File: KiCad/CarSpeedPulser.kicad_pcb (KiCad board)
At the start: 2 copper layers, 48 x 48 mm, 24 parts, among them P1 CONN_01X03, P2 CONN_01X05, Q1 RUE002N02, SW1 RESET, SW2 UP, SW3 DOWN, U1 LPC810, U2 AQM0802A-RN-GBW, U3 NJU7223DL1-33, U4 BD45231G

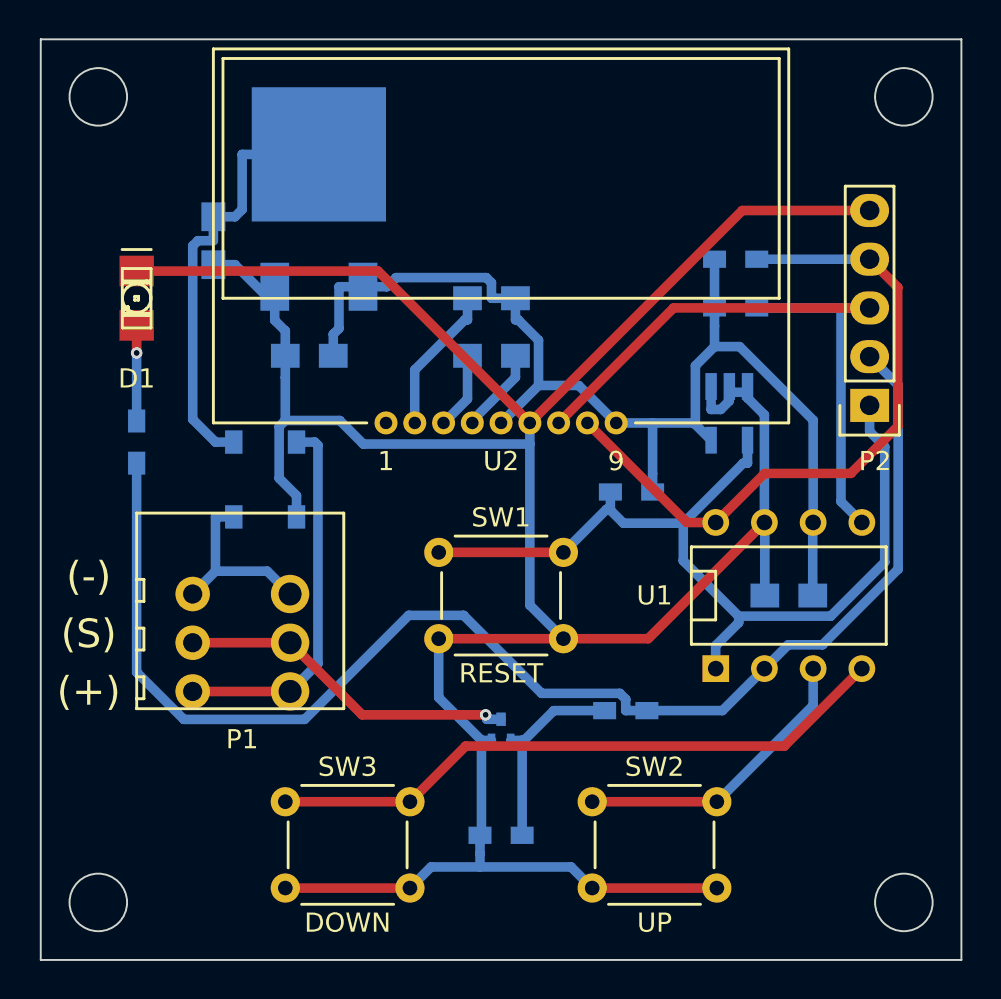
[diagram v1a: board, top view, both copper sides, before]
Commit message: Replaced 3.3V regulator
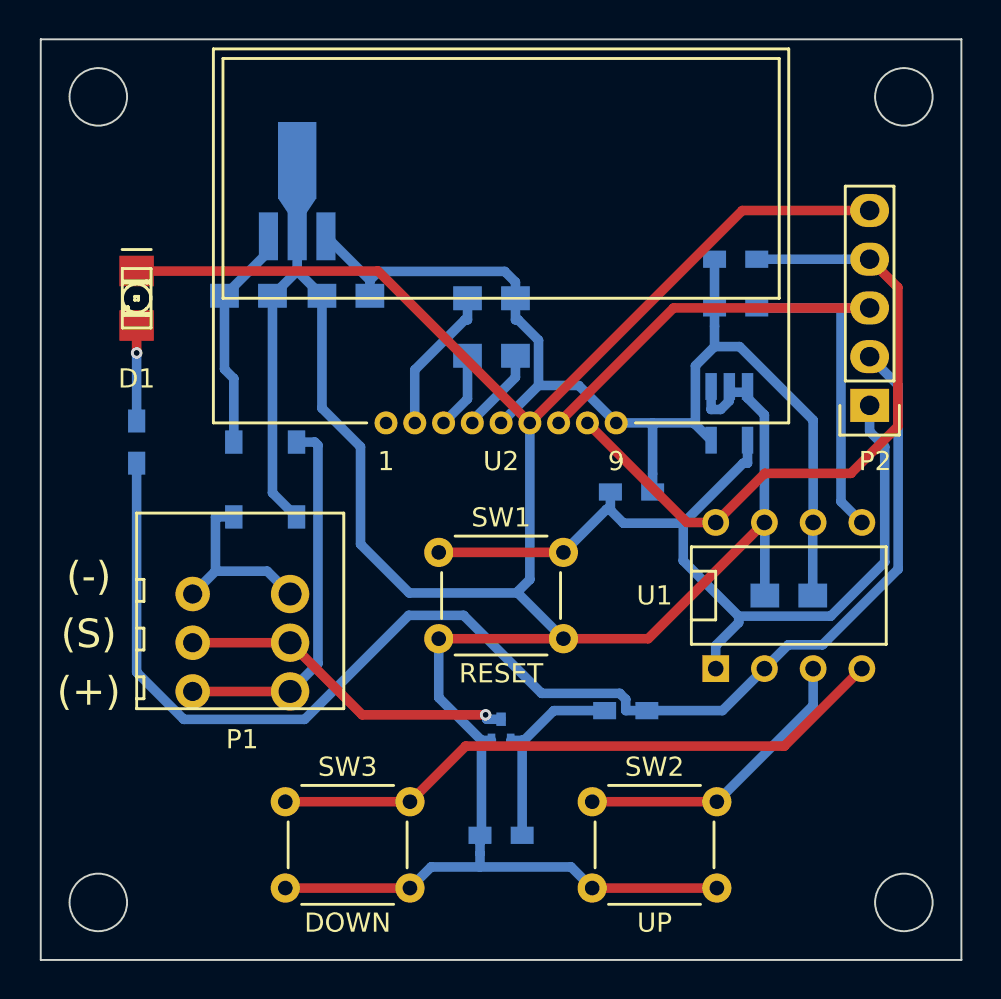
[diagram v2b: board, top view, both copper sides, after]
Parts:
- U3: value NJU7223DL1-33 -> NJM78L33SU3; footprint favorites:TO-252 -> TO_SOT_Packages_SMD:SOT-89-3_Handsoldering
- moved C3 3.67 mm to (41.9, 39.4)
- moved C1 3.40 mm to (36.8, 39.4), turned to 0 degrees
- moved U3 2.55 mm to (39.4, 34.3), turned to 90 degrees
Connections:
- U3 pad 2: /Vin -> /VSS
- U3 pad 3: /VSS -> /Vin
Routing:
- net /VSS: track 160.0 -> 176.6 mm
- net /Vin: track 22.6 -> 11.9 mm
- net VDD: track 60.6 -> 59.4 mm

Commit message: Replaced voltage detector
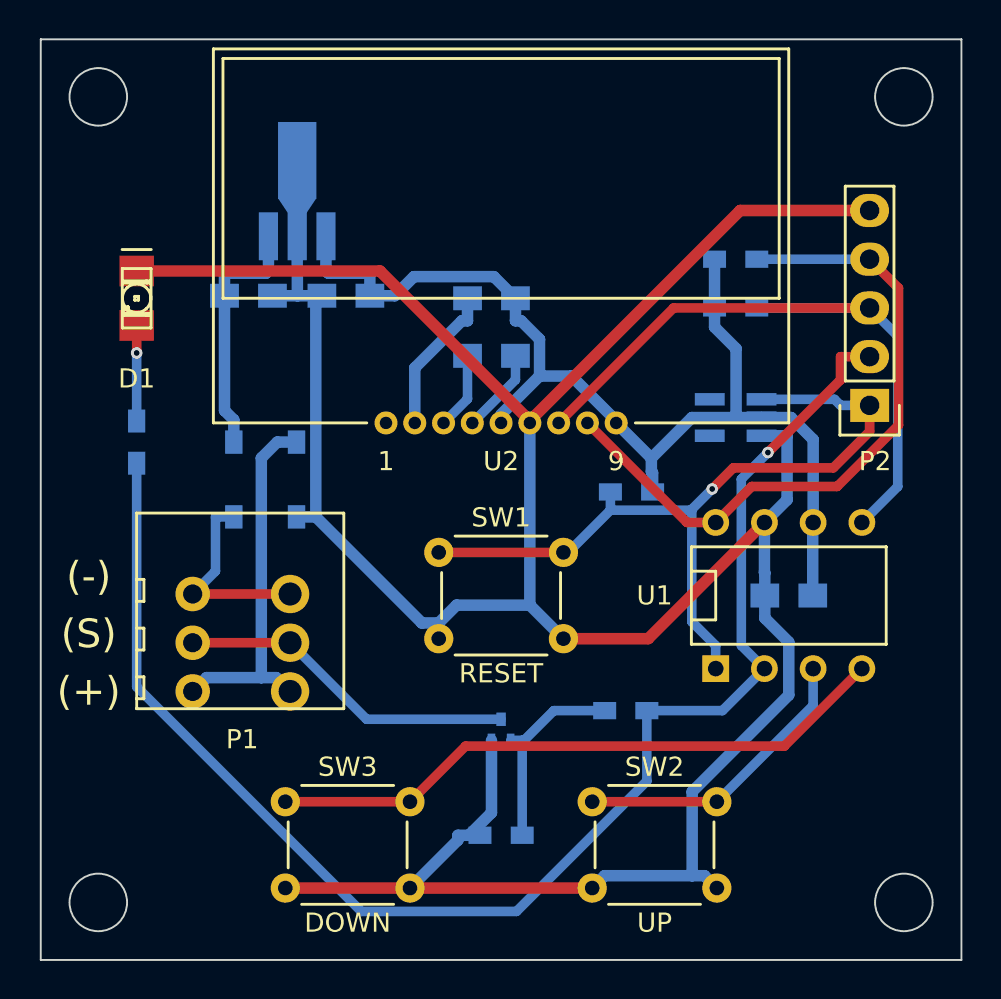
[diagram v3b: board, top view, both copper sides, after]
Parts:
- U4: value BD45231G -> R3111N211A; footprint favorites:SSOP5_Handsoldering -> TO_SOT_Packages_SMD:SOT-23-5_HandSoldering
- moved U4 0.40 mm to (62.2, 45.7), turned to 180 degrees
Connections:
- U4 pad 1: /VSS -> /#RST
- U4 pad 2: /VSS -> VDD
- U4 pad 4: /#RST -> Net-(U4-Pad4)
- U4 pad 5: VDD -> Net-(U4-Pad5)
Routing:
- net /VSS: track 176.6 -> 168.7 mm
- net /PIO0_4: track 71.0 -> 77.1 mm, vias 0 -> 1
- net /#RST: track 47.3 -> 42.0 mm, vias 0 -> 1
- net VDD: track 59.4 -> 57.9 mm
- net /Vin: track 11.9 -> 13.1 mm
- net /SDA: track 36.2 -> 37.2 mm
- net Net-(D3-Pad1): track 9.85 -> 10.5 mm
- net /D: track 17.8 -> 17.7 mm, vias 1 -> 0
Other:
- net class Power: trace_width 0.5 -> 0.6
